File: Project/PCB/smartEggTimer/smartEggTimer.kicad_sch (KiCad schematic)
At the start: 62 parts, among them J1 Conn_01x05_Pin, J2 Conn_01x02_Pin, J3 Conn_01x02_Pin, J4 Conn_01x02_Pin, SW1 SW_Push_Dual, SW2 RotaryEncoder, SW3 SW_Push_Dual, SW4 SW_Push_Dual, SW5 SW_Push_Dual, SW6 SW_Push_Dual, SW7 SW_SPDT, U1 STM32F103RET6, U2 XC6206P332MR-G

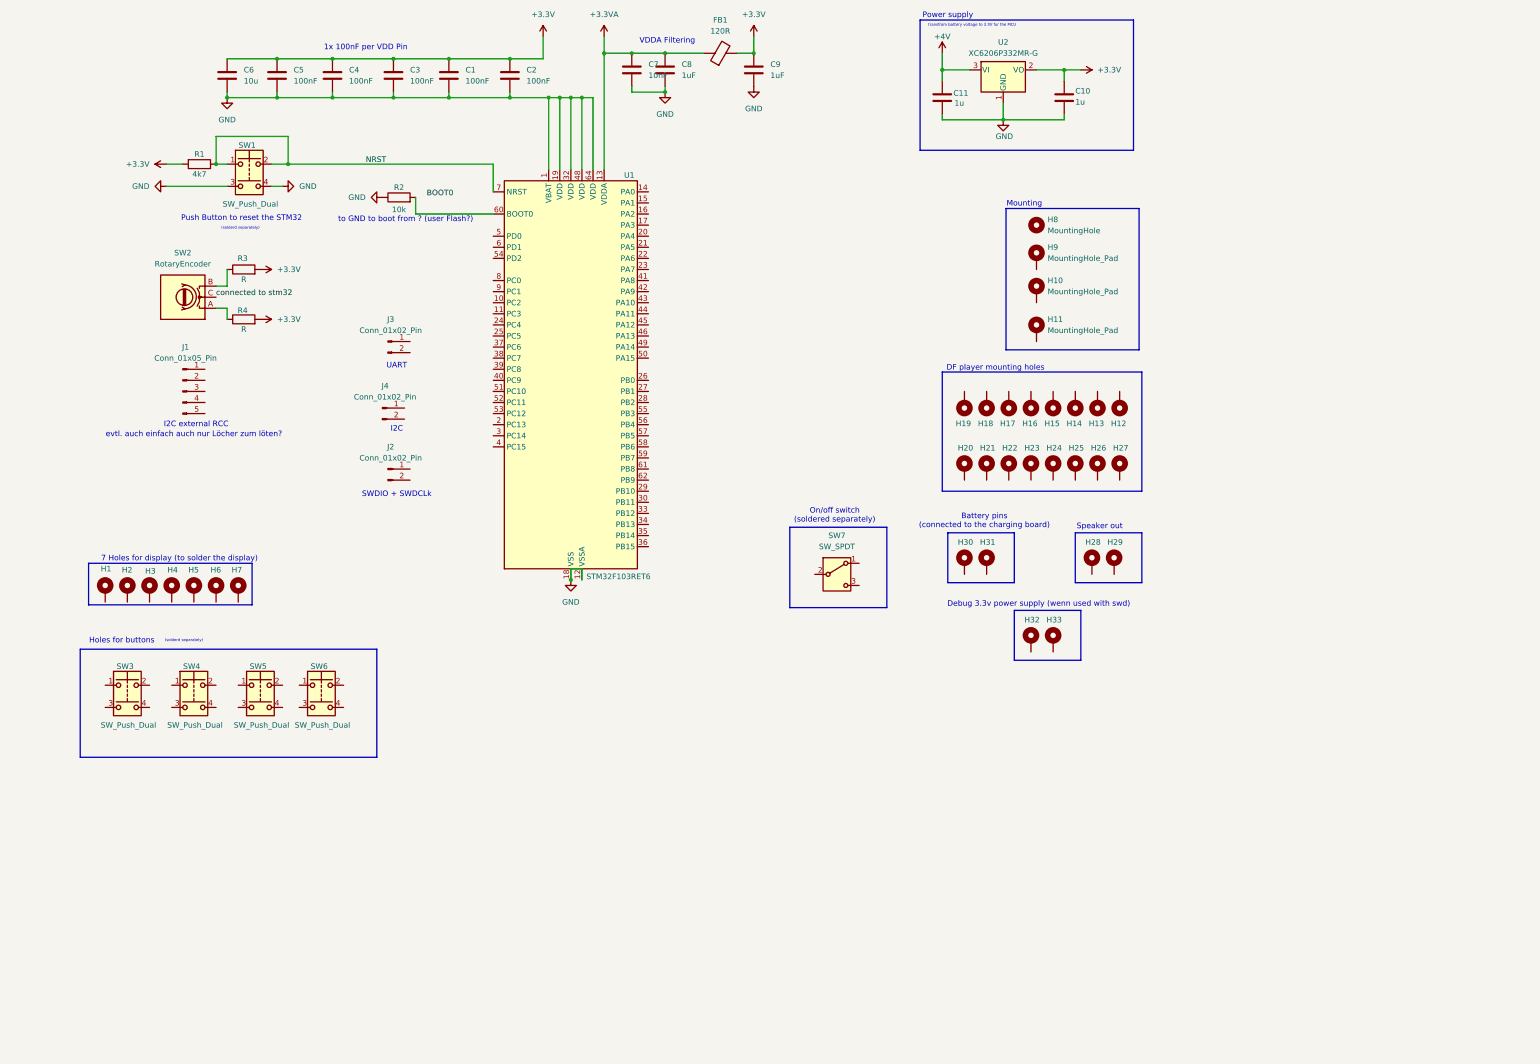
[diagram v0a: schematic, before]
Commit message: connect parts to pins
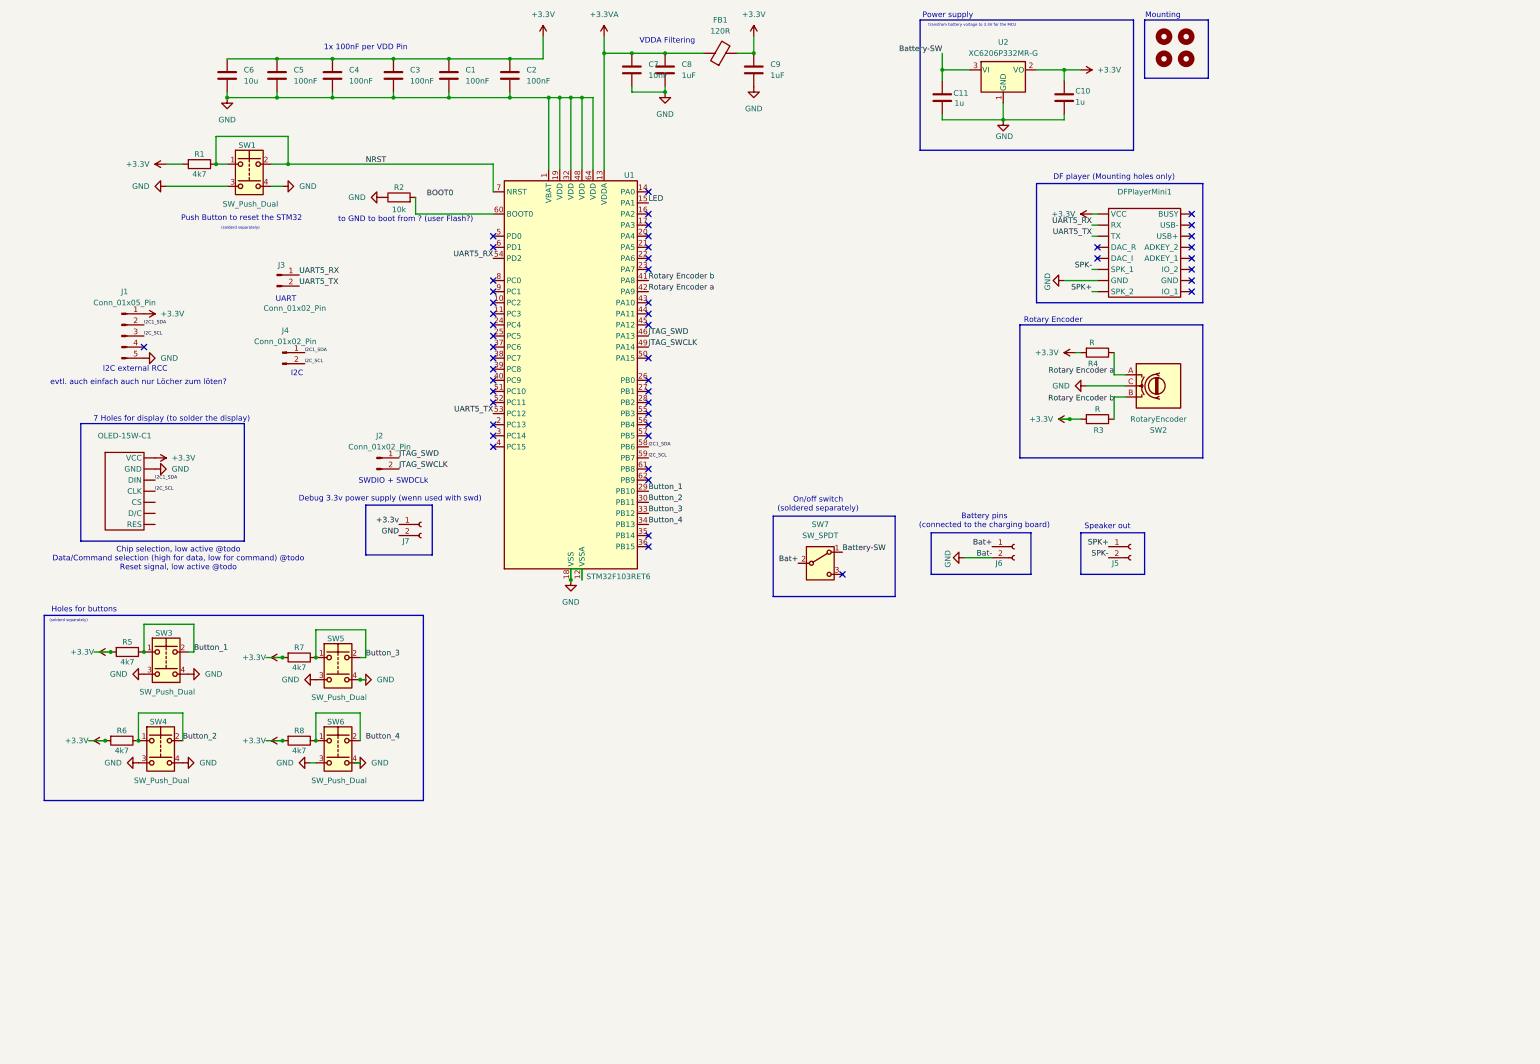
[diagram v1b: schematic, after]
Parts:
- removed H1, H10, H11, H12, H13, H14, H15, H16, H17, H18, H19, H2, H20, H21, H22, H23, H24, H25, H26, H27, H28, H29, H3, H30, H31, H32, H33, H4, H5, H6, H7, H9: MountingHole_Pad, symbol Mechanical:MountingHole_Pad
- added DFPlayerMini1: ~, symbol custom-parts:DFPlayer_Mini
- added H1, H2, H3: MountingHole, symbol Mechanical:MountingHole
- added J5, J6, J7: Conn_01x02_Socket, symbol Connector:Conn_01x02_Socket
- added OLED-15W-C1: ~, symbol custom-parts:OLED-15W-C
- added R5, R6, R7, R8: 4k7, symbol Device:R
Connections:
- net +4V is gone; now on net Battery-SW: C11.1, U2.3 (VI)
- net connected to stm32 is gone; now on net GND: SW2.C
- net +3.3V: now also J1.1 (Pin_1), DFPlayerMini1. (VCC), OLED-15W-C1. (VCC), R5.2, R6.2, R7.2, R8.2
- net GND: now also J1.5 (Pin_5), SW3.3, SW3.4, SW4.3, SW4.4, SW5.3, SW5.4, SW6.3, SW6.4, DFPlayerMini1. (VCC), J6.2 (Pin_2), J7.2 (Pin_2), OLED-15W-C1. (VCC)
- net JTAG_SWD: now reaches J2.1 (Pin_1)
- net JTAG_SWD: now also U1.46 (PA13)
- net JTAG_SWCLK: now reaches J2.2 (Pin_2)
- net JTAG_SWCLK: now also U1.49 (PA14)
- net I2C1_SDA: now reaches J4.1 (Pin_1)
- net I2C1_SDA: now also J1.2 (Pin_2), U1.58 (PB6), OLED-15W-C1. (VCC)
- net I2C_SCL: now reaches J4.2 (Pin_2)
- net I2C_SCL: now also J1.3 (Pin_3), U1.59 (PB7), OLED-15W-C1. (VCC)
- net at SW6.1: now also SW6.2, R8.1
- net Rotary Encoder b: now reaches R3.1, SW2.B
- net Rotary Encoder b: now also U1.41 (PA8)
- net LED: now reaches U1.15 (PA1)
- net Button_1: now reaches U1.29 (PB10)
- net Button_1: now also SW3.1, SW3.2, R5.1
- net Button_2: now reaches U1.30 (PB11)
- net Button_2: now also SW4.1, SW4.2, R6.1
- net Button_3: now reaches U1.33 (PB12)
- net Button_3: now also SW5.1, SW5.2, R7.1
- net Button_4: now reaches U1.34 (PB13)
- net Rotary Encoder a: now reaches U1.42 (PA9)
- net Rotary Encoder a: now also R4.1, SW2.A
- net UART5_TX: now reaches U1.53 (PC12)
- net UART5_TX: now also J3.2 (Pin_2), DFPlayerMini1. (VCC)
- net UART5_RX: now reaches U1.54 (PD2)
- net UART5_RX: now also J3.1 (Pin_1), DFPlayerMini1. (VCC)
- net Battery-SW: now reaches SW7.1 (A)
- net Bat+: now reaches SW7.2 (B)
- net Bat+: now also J6.1 (Pin_1)
- new net +3.3v: J7.1 (Pin_1)
- new net SPK+: DFPlayerMini1. (VCC), J5.1 (Pin_1)
- new net SPK-: DFPlayerMini1. (VCC), J5.2 (Pin_2)
- no-connect marks 0 -> 50
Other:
- note added: "Chip selection, low active @todo Data/Command selection (high for data, low for command) @todo Reset signal, low active @todo"
- note added: "DF player (Mounting holes only)"
- note added: "Rotary Encoder"
- note removed: "DF player mounting holes"
- title: (none) -> SmartEggTimer
- moved on the sheet: J1, J2, J3, J4, R3, R4, SW2, SW3, SW4, SW5, SW6, SW7

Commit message: add footprints for DFPlayer and fix error
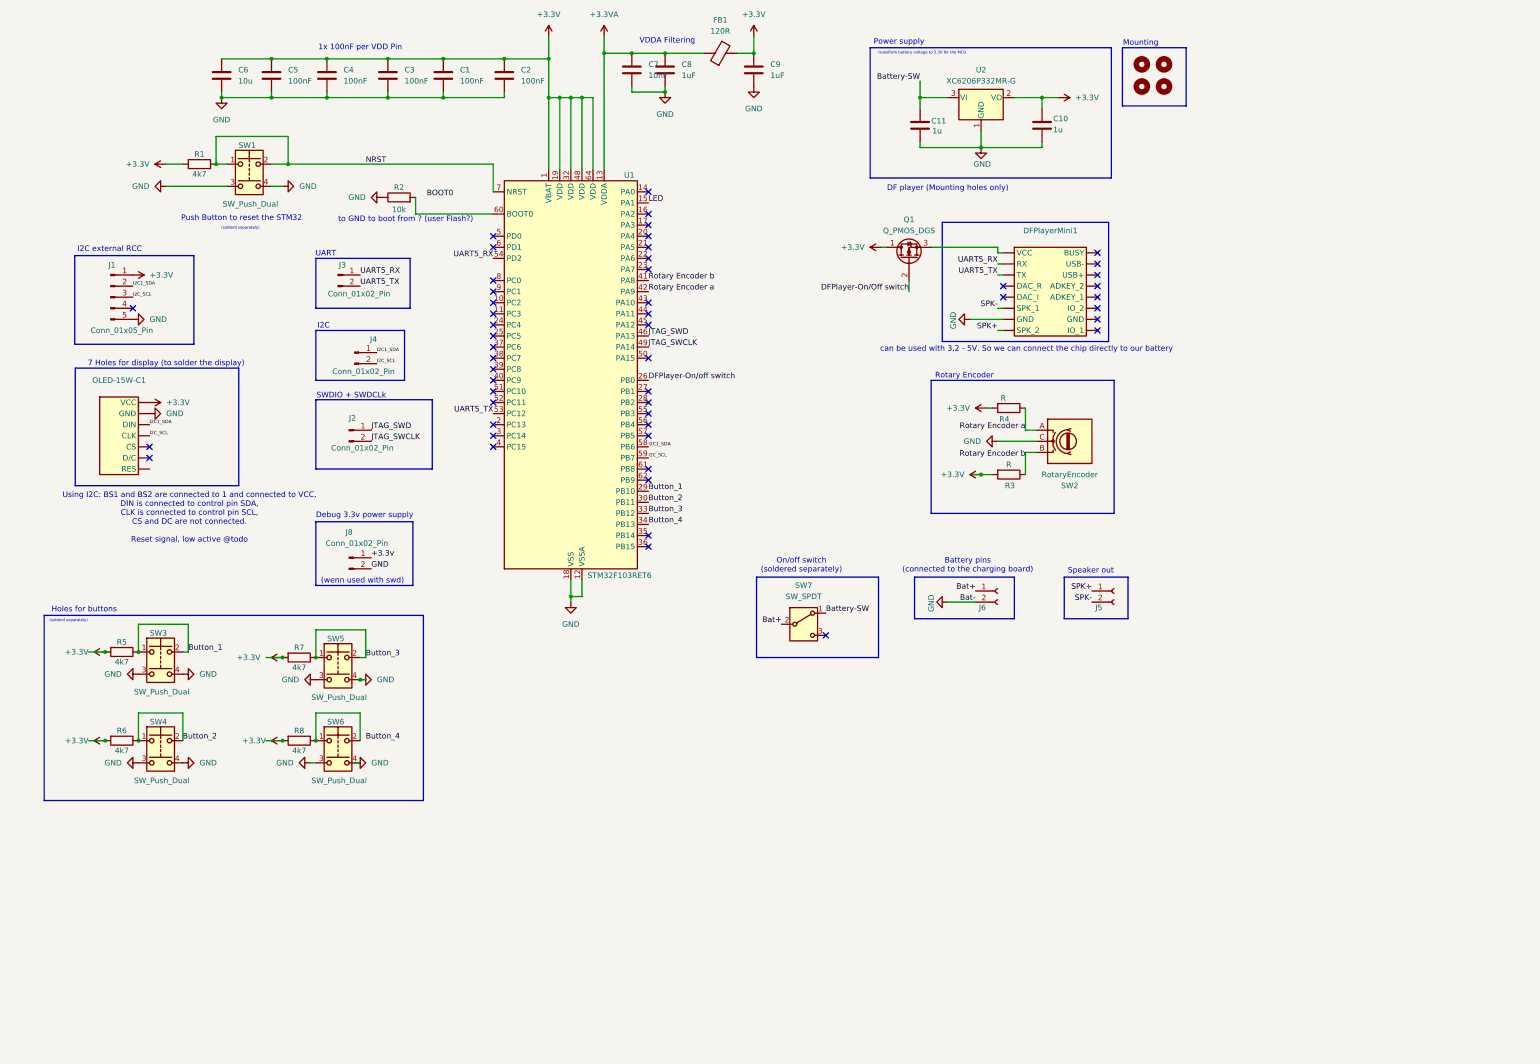
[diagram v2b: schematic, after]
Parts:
- removed J7: Conn_01x02_Socket, symbol Connector:Conn_01x02_Socket
- added J8: Conn_01x02_Pin, Connector_PinHeader_2.54mm:PinHeader_1x01_P2.54mm_Vertical, symbol Connector:Conn_01x02_Pin
- added Q1: Q_PMOS_DGS, symbol Device:Q_PMOS_DGS
- C1, C2, C3, C4, C5: footprint (none) -> Capacitor_SMD:C_0402_1005Metric
- C10, C11, C6, C8, C9: footprint (none) -> Capacitor_SMD:C_0603_1608Metric
- C7: footprint (none) -> Capacitor_SMD:C_0805_2012Metric
- DFPlayerMini1: footprint (none) -> custom-parts:DFplayer-Mini
- J1: footprint (none) -> Connector_PinHeader_2.54mm:PinHeader_1x05_P2.54mm_Vertical
- J2, J3, J4: footprint (none) -> Connector_PinHeader_2.54mm:PinHeader_1x01_P2.54mm_Vertical
- OLED-15W-C1: footprint (none) -> Connector_PinSocket_2.54mm:PinSocket_1x07_P2.54mm_Vertical
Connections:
- net +3.3V: now also U1.1 (VBAT), U1.19 (VDD), U1.32 (VDD), U1.48 (VDD), U1.64 (VDD), Q1.1 (D); no longer DFPlayerMini1. (VCC)
- net +3.3v: now also J8.1 (Pin_1)
- net GND: now also J8.2 (Pin_2); no longer U1.1 (VBAT), U1.19 (VDD), U1.32 (VDD), U1.48 (VDD), U1.64 (VDD)
- net DFPlayer-On/off switch: now reaches U1.26 (PB0)
- new net: DFPlayerMini1. (VCC), Q1.3 (S)
- new net DFPlayer-On/Off switch: Q1.2 (G)
- no-connect marks 50 -> 51
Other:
- note added: "(wenn used with swd)"
- note added: "Debug 3.3v power supply"
- note added: "Using I2C: BS1 and BS2 are connected to 1 and connected to VCC, DIN is connected to control pin SDA, CLK is connected to control pin SCL, CS and DC are not connected. Reset signal, low active @todo"
- note added: "can be used with 3,2 - 5V. So we can connect the chip directly to our battery"
- note removed: "Chip selection, low active @todo Data/Command selection (high for data, low for command) @todo Reset signal, low active @todo"
- note removed: "Debug 3.3v power supply (wenn used with swd)"
- note removed: "evtl. auch einfach auch nur Löcher zum löten?"
- moved on the sheet: C1, C10, C11, C2, C3, C4, C5, C6, J1, J2, J3, J4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

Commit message: fix buttons, finish rotary encoder, add battery indicator
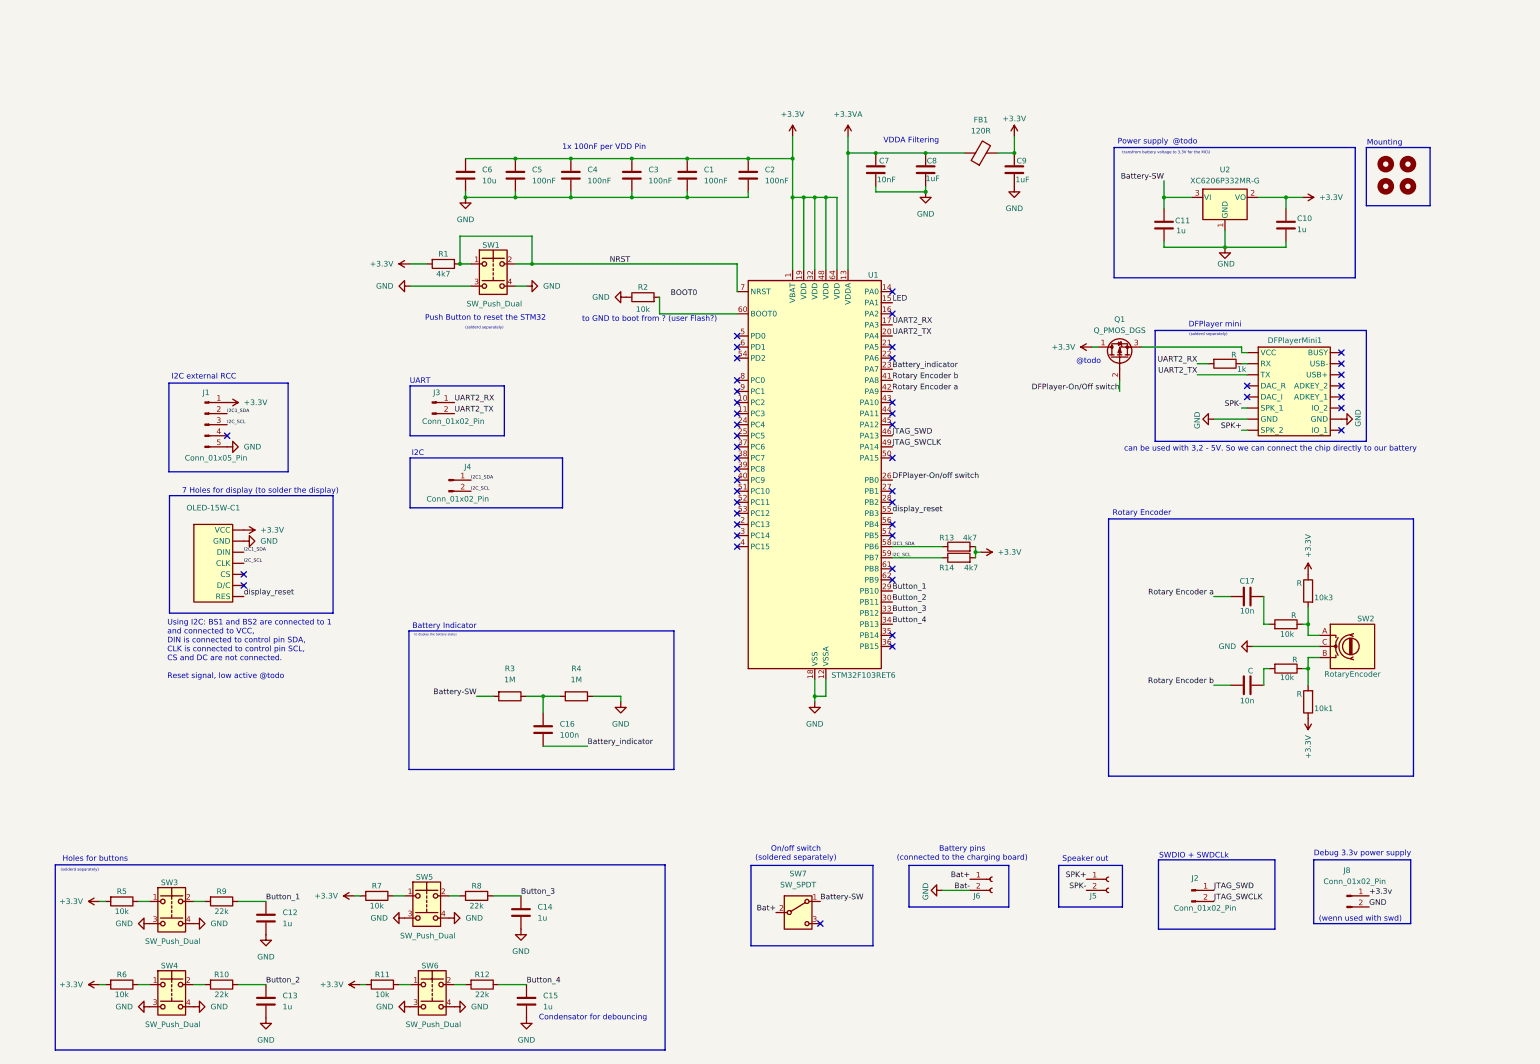
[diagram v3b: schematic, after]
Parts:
- added 10k, 10k1, 10k3, 1k: R, symbol Device:R
- added 10n: C, symbol Device:C
- added C12, C13, C14, C15: 1u, symbol Device:C
- added C16: 100n, symbol Device:C
- added C17: 10n, symbol Device:C
- added R10, R12, R9: 22k, symbol Device:R
- added R11: 10k, symbol Device:R
- added R13, R14: 4k7, symbol Device:R
- added R3: 1M, symbol Device:R
- R4: value R -> 1M
- R5, R6, R7: value 4k7 -> 10k
- R8: value 4k7 -> 22k
- renumbered R3 to 10k
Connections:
- net +3.3V: now also 10k1.1, 10k3.1, R11.2, R13.2, R14.2; no longer 10k.2, R4.2, R8.2
- net Battery-SW: now also R3.2
- net Button_1: now also C12.1, R9.1; no longer R5.1, SW3.1, SW3.2
- net Button_2: now also C13.1, R10.1; no longer R6.1, SW4.1, SW4.2
- net Button_3: now also R8.1, C14.1; no longer R7.1, SW5.1, SW5.2
- net Button_4: now also C15.1, R12.1
- net GND: now also R4.1, C12.2, C13.2, C14.2, C15.2
- net I2C1_SDA: now also R13.1
- net I2C_SCL: now also R14.1
- net Rotary Encoder a: now also C17.2; no longer R4.1, SW2.A
- net Rotary Encoder b: now also 10n.2; no longer 10k.1, SW2.B
- net display_reset: now reaches OLED-15W-C1. (VCC)
- net display_reset: now also U1.55 (PB3)
- net UART2_RX: now reaches U1.17 (PA3)
- net UART2_RX: now also J3.1 (Pin_1), 1k.2
- net UART2_TX: now reaches U1.20 (PA4)
- net UART2_TX: now also DFPlayerMini1. (VCC), J3.2 (Pin_2)
- net Battery_indicator: now reaches U1.23 (PA7)
- net Battery_indicator: now also C16.2
- removed net UART5_RX: DFPlayerMini1. (VCC), J3.1 (Pin_1), U1.54 (PD2)
- removed net UART5_TX: DFPlayerMini1. (VCC), J3.2 (Pin_2), U1.53 (PC12)
- new net: R9.2, SW3.2
- new net: 10k.1, 10k3.2, SW2.A
- new net: 1k.1, DFPlayerMini1. (VCC)
- new net: R10.2, SW4.2
- new net: R7.1, SW5.1
- new net: R8.2, SW5.2
- new net: C16.1, R3.1, R4.2
- new net: R6.1, SW4.1
- new net: 10k.1, 10k1.2, SW2.B
- new net: 10k.2, 10n.1
- new net: R5.1, SW3.1
- new net: 10k.2, C17.1
- new net: R11.1, SW6.1
- new net: R12.2, SW6.2
- no-connect marks 51 -> 48
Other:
- note added: "@todo"
- note added: "Battery Indicator"
- note added: "Condensator for debouncing"
- note added: "DFPlayer mini"
- note added: "to display the battery status"
- note removed: "DF player (Mounting holes only)"
- moved on the sheet: 10k, C1, C10, C11, C2, C3, C4, C5, C6, C7, C8, C9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
